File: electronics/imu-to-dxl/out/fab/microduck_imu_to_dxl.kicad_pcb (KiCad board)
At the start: 2 copper layers, 34 x 24 mm, 24 parts, among them J1 DXL bus (B3B-EH-A), J2 DXL bus (B3B-EH-A), J3 DXL bus (B3B-EH-A), U1 LSM6DSV16X, U2 STM32G031F6P6, U3 74LVC1G125, U4 LP2985A-33DBVR

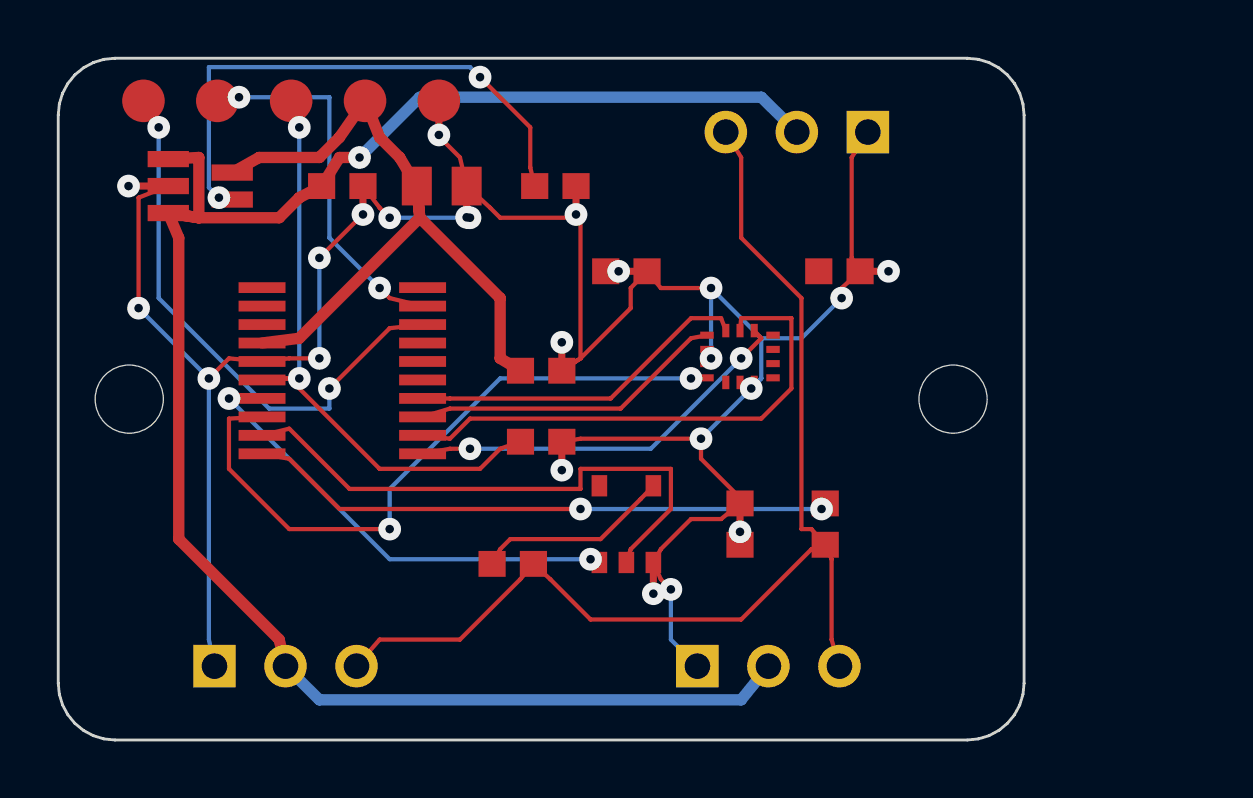
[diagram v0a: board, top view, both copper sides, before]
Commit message: lane D: imu_to_dxl routed 40/53 with three named open nets, and the stub trade-off is measured
Three runs on the same layout, same budgets, only the GND stub vias changing:
  10 stubs -> 43/53 routed, 7 FAIL (two 'hole-to-hole via GND / via GND' and a
              GND track 0.000 mm from U4.1)
   9 stubs -> 45/53 routed, 5 FAIL
   0 stubs -> 40/53 routed, 3 FAIL, every one of them 'unrouted'
The stubs buy routed connections and pay for them in fixed obstacles on a
40 x 22 mm board carrying 24 parts. The version shipped is the 0-stub one:
fewer rule violations and no clearance or hole-to-hole defects, only open
connections - GND 8, V3V3 5, IMU_INT1 1.

PCB-PACKAGE.html section 5.9 carries the table and says what would fix it:
more board, which costs nothing at either fab up to 100 x 100 mm, but which
would trade a routing failure for a fit risk because the trunk cavity is not
measured - only the site's neighbours are (E11).
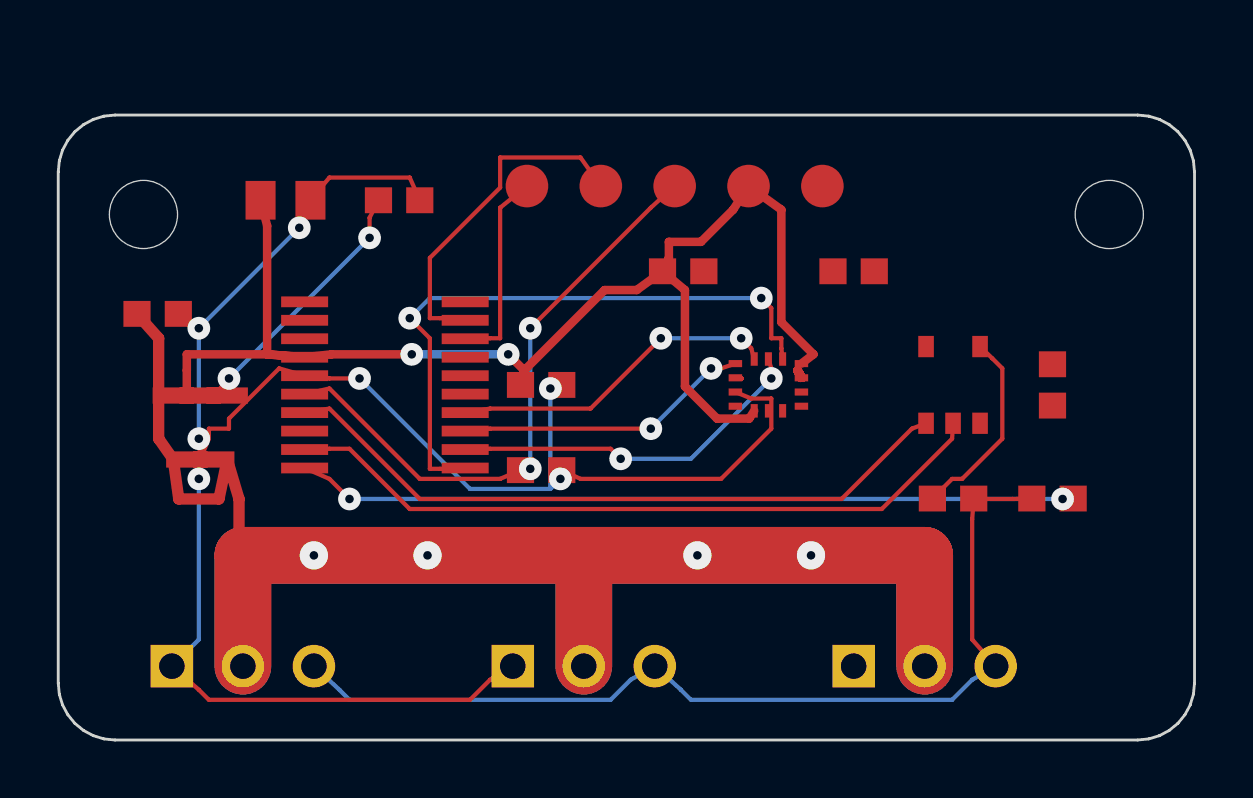
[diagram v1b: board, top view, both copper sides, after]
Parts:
- moved J3 19.3 mm to (30.5, -2.60), turned to 0 degrees
- moved R1 15.7 mm to (31.5, -8.50)
- moved TP2 13.8 mm to (19.1, -19.5)
- moved TP1 13.8 mm to (16.5, -19.5)
- moved TP3 13.8 mm to (21.7, -19.5)
- moved TP4 13.8 mm to (24.3, -19.5)
- moved TP5 13.8 mm to (26.9, -19.5)
- moved U3 12.5 mm to (31.5, -12.5)
- moved C7 12.0 mm to (35.0, -12.5)
- moved H2 8.51 mm to (37.0, -18.5)
- moved U4 8.50 mm to (5.00, -11.0), turned to 270 degrees
- moved R2 8.05 mm to (35.0, -8.50), turned to 0 degrees
- moved C1 7.91 mm to (3.50, -15.0)
- moved H1 6.52 mm to (3.00, -18.5)
- moved J2 6.50 mm to (18.5, -2.60)
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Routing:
- net V3V3: track 25.9 -> 94.9 mm, vias 0 -> 2
- net IMU_INT1: track 23.7 -> 0.00 mm, vias 2 -> 0
- net SERVO_V: track 64.3 -> 85.0 mm, vias 1 -> 4
- net GND: track 101.3 -> 121.0 mm, vias 23 -> 7
- net SWDIO: track 19.6 -> 7.04 mm, vias 2 -> 0
- net BYPASS: track 19.5 -> 9.20 mm
- net SPI_NSS: track 13.9 -> 22.2 mm
- net DIR: track 16.6 -> 24.3 mm, vias 2 -> 0
- net MCU_RX: track 20.7 -> 27.4 mm
- net dxl/DATA: track 40.4 -> 34.0 mm
- net SPI_SCK: track 18.4 -> 12.8 mm, vias 0 -> 2
- net MCU_TX: track 19.9 -> 25.2 mm
- net SWCLK: track 13.1 -> 12.0 mm, vias 2 -> 0
- net SPI_MISO: track 11.1 -> 10.4 mm, vias 0 -> 2
- net SPI_MOSI: track 12.1 -> 11.6 mm, vias 0 -> 2
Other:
- board size 34 x 24 mm -> 40 x 22 mm
